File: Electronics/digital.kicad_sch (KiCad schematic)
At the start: 24 parts, among them IC1 ICM-42670-P, J2 10137065-00021LF, U3 ESP32-S3-WROOM-1

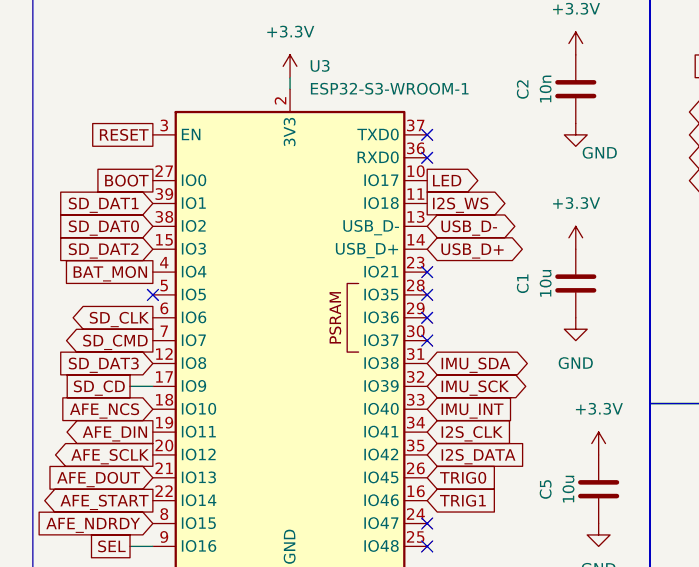
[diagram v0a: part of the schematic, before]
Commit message: [Electronics] version 1.0.0 of the PCB released.\n [Firmware] Added ICS43434 drivers and prepared code for reestructuration
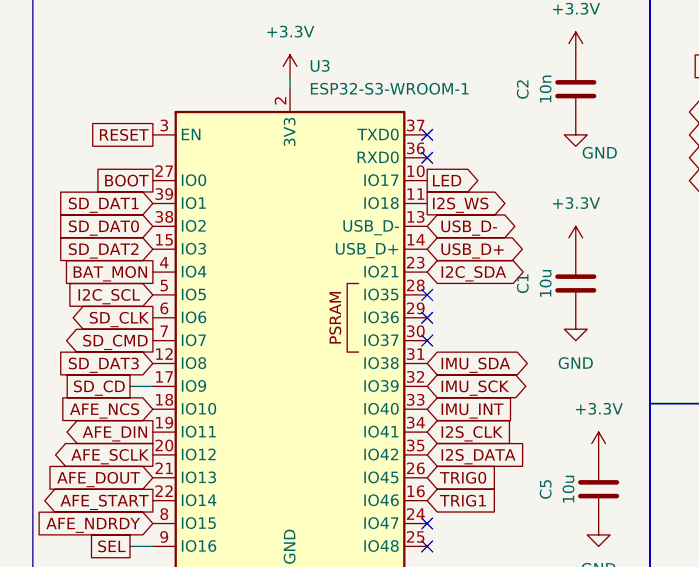
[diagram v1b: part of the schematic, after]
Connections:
- net I2C_SDA: now reaches U3.23 (IO21)
- net I2C_SCL: now reaches U3.5 (IO5)
- no-connect marks 25 -> 23
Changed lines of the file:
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@@
-	)
-	(no_connect
-		(at 25.4 52.07)
 	)
 	(no_connect
@@
 	(no_connect
 		(at 55.88 54.61)
-	)
-	(no_connect
-		(at 55.88 49.53)
 	)
 	(no_connect
@@
 		)
 	)
+	(global_label "I2C_SCL"
+		(shape input)
+		(at 25.4 52.07 180)
+		(fields_autoplaced yes)
+		(effects
+			(font
+				(size 1.27 1.27)
+			)
+			(justify right)
+		)
+		(property "Intersheetrefs" "${INTERSHEET_REFS}"
+			(at 14.8553 52.07 0)
+			(hide yes)
+			(show_name no)
+			(do_not_autoplace no)
+			(effects
+				(font
+					(size 1.27 1.27)
+				)
+				(justify right)
+			)
+		)
+	)
 	(global_label "IMU_INT"
 		(shape output)
@@
 			)
 		)
+	)
+	(global_label "I2C_SDA"
+		(shape bidirectional)
+		(at 55.88 49.53 0)
+		(fields_autoplaced yes)
+		(effects
+			(font
+				(size 1.27 1.27)
+			)
+			(justify left)
+		)
+		(property "Intersheetrefs" "${INTERSHEET_REFS}"
+			(at 67.5965 49.53 0)
+			(hide yes)
+			(show_name no)
+			(do_not_autoplace no)
+			(effects
+				(font
+					(size 1.27 1.27)
+				)
+				(justify left)
+			)
+		)
